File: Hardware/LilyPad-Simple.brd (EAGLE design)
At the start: 50 x 50 mm, 43 parts, among them U1 ATMEGA328P_TQFP, U2 MCP73831, U3 MIC5219 3.3V, Y1 8MHZ

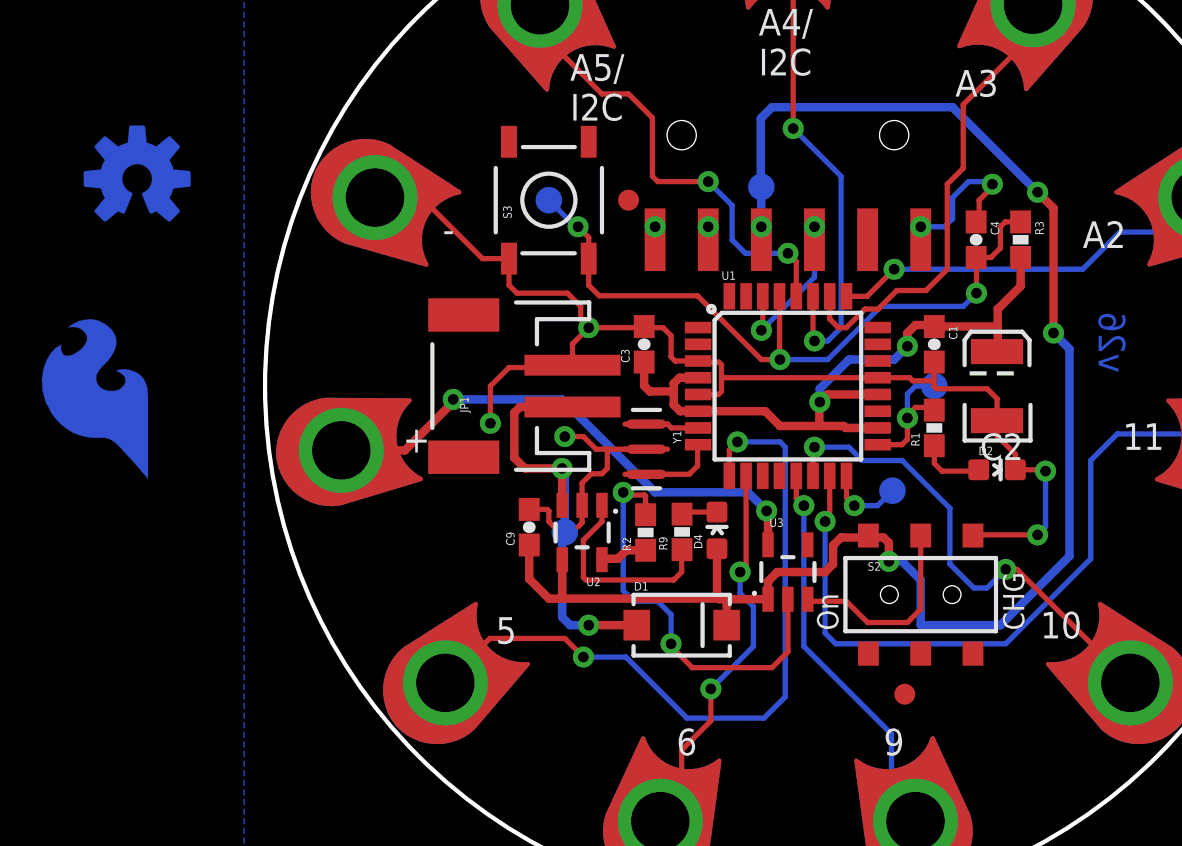
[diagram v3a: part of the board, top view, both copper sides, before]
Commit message: fixed 3.3 routing
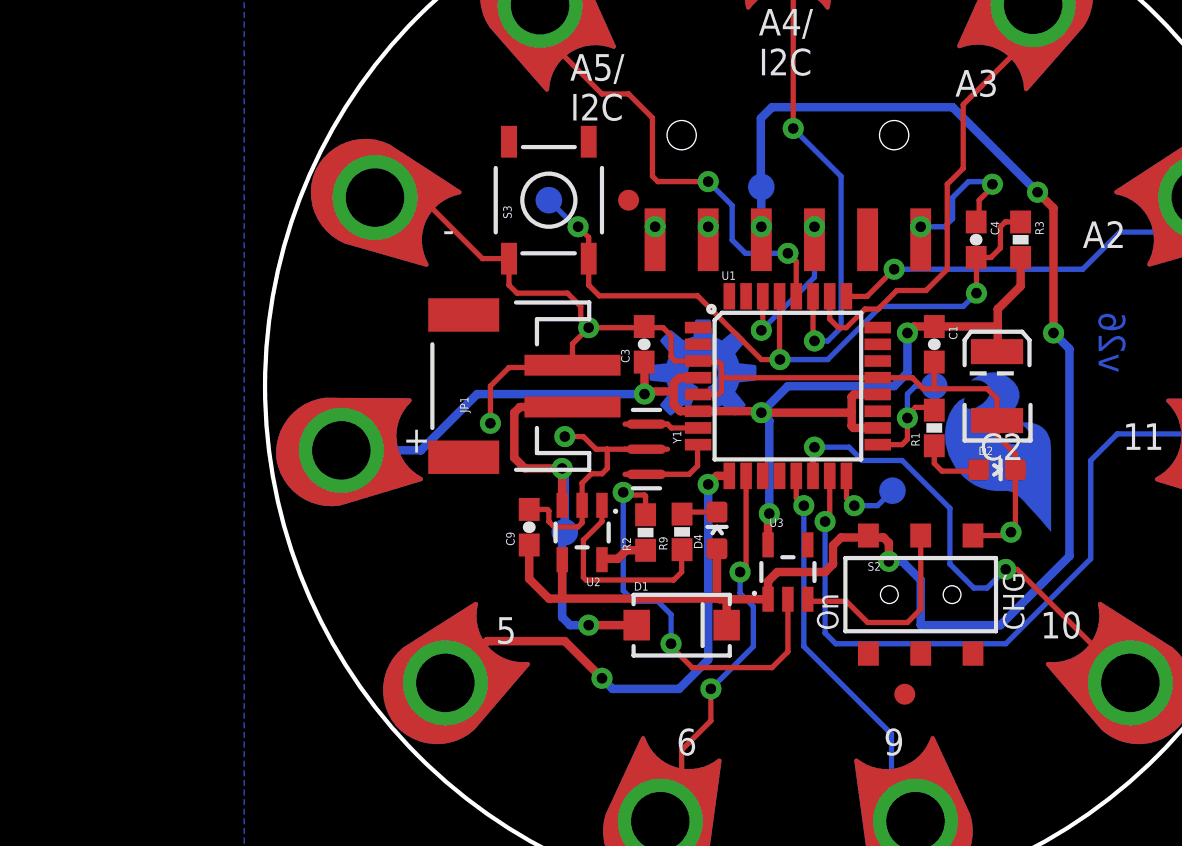
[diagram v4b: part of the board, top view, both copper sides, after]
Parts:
- moved LOGO2 43.3 mm to (13.1, -7.11)
- moved LOGO1 28.6 mm to (-4.06, 0.64)
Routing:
- net D5: track 35.2 -> 24.9 mm
- net GND: track 92.1 -> 90.2 mm, vias 9 -> 8
- net 3.3V: track 60.3 -> 59.1 mm

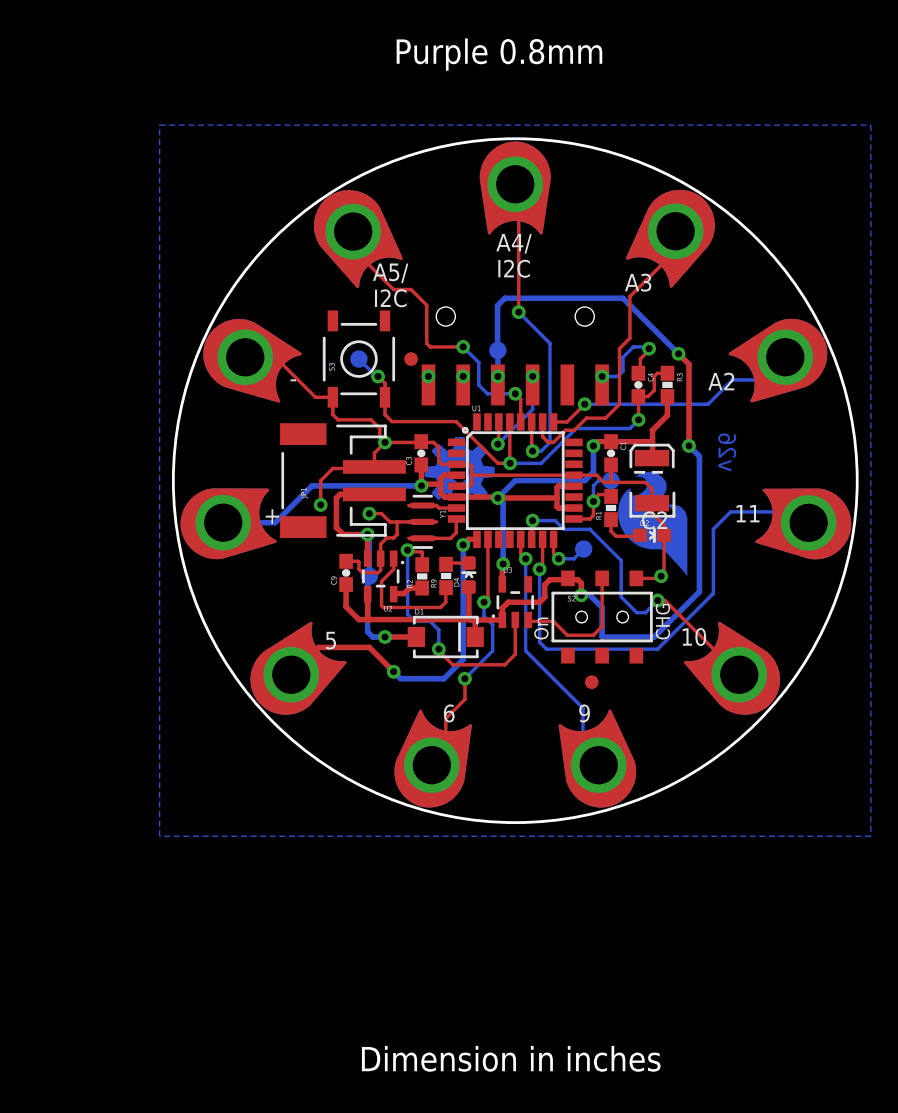
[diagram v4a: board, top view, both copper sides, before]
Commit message: Checklist edits
Silk edited, TX and RX reconnected
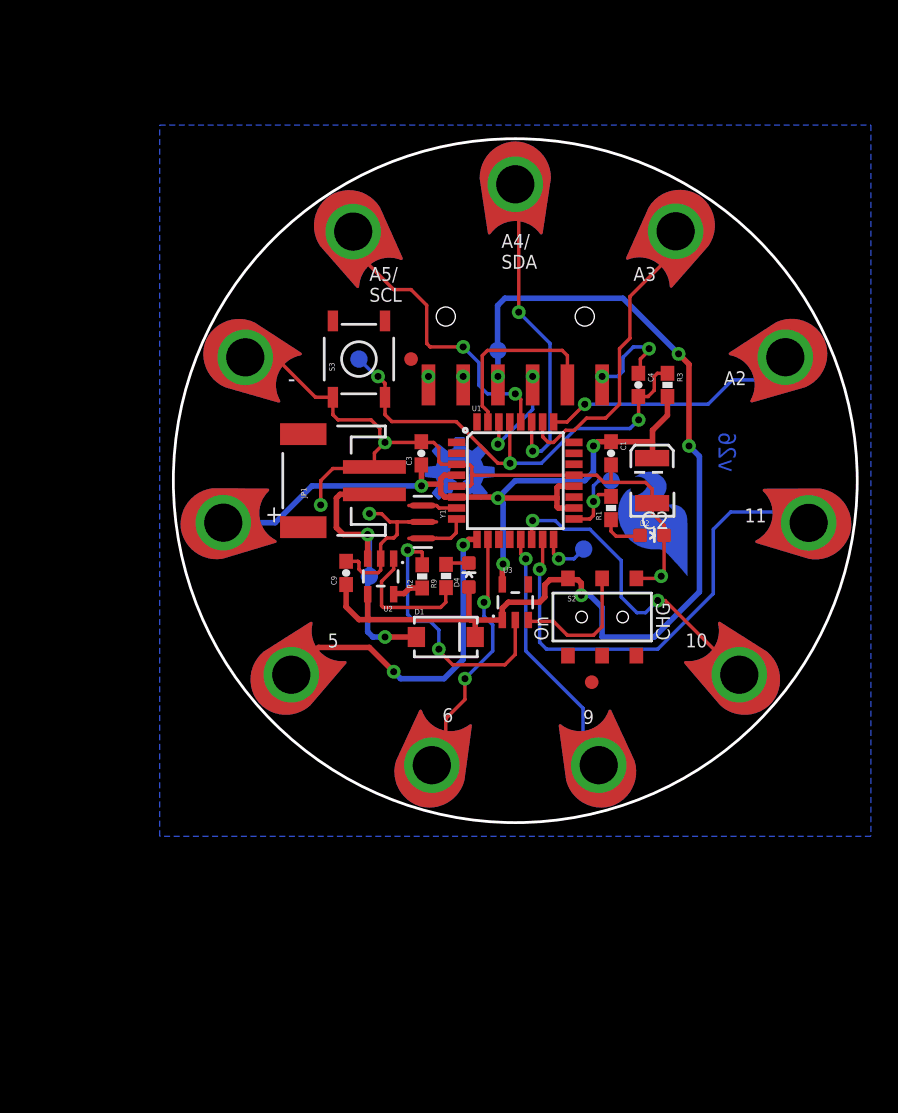
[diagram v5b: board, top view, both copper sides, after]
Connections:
- net DTR: now also JP2.1
- net RXI: now also JP2.3
- net TXO: now also JP2.2
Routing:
- net TXO: track 0.00 -> 13.7 mm
- net RXI: track 7.66 -> 8.28 mm
- net DTR: track 7.17 -> 7.79 mm
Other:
- board text added: "A4/ SDA"
- board text added: "A5/ SCL"
- board text removed: "A4/ I2C"
- board text removed: "A5/ I2C"
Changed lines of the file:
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@@
 <text x="-88.9" y="-3.81" size="1.778" layer="51" font="vector" ratio="15">Dia Campbell</text>
 <text x="14.859" y="0.635" size="1.27" layer="16" font="vector" ratio="15" rot="MR90">v26</text>
-<text x="-18.415" y="-3.175" size="1.27" layer="21" font="vector" ratio="15">+</text>
-<text x="-16.51" y="6.858" size="1.27" layer="21" font="vector" ratio="15">-</text>
-<text x="-10.414" y="12.7" size="1.27" layer="21" font="vector" ratio="15">A5/
-I2C</text>
-<text x="-1.397" y="14.859" size="1.27" layer="21" font="vector" ratio="15">A4/
-I2C</text>
-<text x="8.001" y="13.843" size="1.27" layer="21" font="vector" ratio="15">A3</text>
-<text x="14.097" y="6.604" size="1.27" layer="21" font="vector" ratio="15">A2</text>
-<text x="16.002" y="-3.048" size="1.27" layer="21" font="vector" ratio="15">11</text>
-<text x="12.065" y="-12.065" size="1.27" layer="21" font="vector" ratio="15">10</text>
-<text x="4.572" y="-17.653" size="1.27" layer="21" font="vector" ratio="15">9</text>
-<text x="-5.334" y="-17.653" size="1.27" layer="21" font="vector" ratio="15">6</text>
-<text x="-13.97" y="-12.319" size="1.27" layer="21" font="vector" ratio="15">5</text>
+<text x="-18.288" y="-3.048" size="1.27" layer="21" font="vector" ratio="15">+</text>
+<text x="-16.637" y="6.858" size="1.27" layer="21" font="vector" ratio="15">-</text>
+<text x="-10.668" y="13.081" size="1.016" layer="21" font="vector" ratio="15">A5/
+SCL</text>
+<text x="-1.016" y="15.494" size="1.016" layer="21" font="vector" ratio="15">A4/
+SDA</text>
+<text x="8.636" y="14.605" size="1.016" layer="21" font="vector" ratio="15">A3</text>
+<text x="15.24" y="6.985" size="1.016" layer="21" font="vector" ratio="15">A2</text>
+<text x="16.764" y="-3.048" size="1.016" layer="21" font="vector" ratio="15">11</text>
+<text x="12.446" y="-12.192" size="1.016" layer="21" font="vector" ratio="15">10</text>
+<text x="4.953" y="-17.78" size="1.016" layer="21" font="vector" ratio="15">9</text>
+<text x="-5.334" y="-17.653" size="1.016" layer="21" font="vector" ratio="15">6</text>
+<text x="-13.716" y="-12.192" size="1.016" layer="21" font="vector" ratio="15">5</text>
 <text x="2.413" y="-11.684" size="1.016" layer="21" font="vector" ratio="15" rot="R90">On</text>
 <text x="10.287" y="-8.89" size="1.016" layer="21" font="vector" ratio="15" rot="R270">CHG</text>
 <dimension x1="25" y1="0" x2="-25" y2="0" x3="0" y3="-38.1" textsize="1.778" textratio="15" layer="47" dtype="diameter" unit="inch"/>
-<text x="-11.43" y="-43.18" size="1.778" layer="20" font="vector" ratio="15">Dimension in inches</text>
-<text x="-8.89" y="30.48" size="1.778" layer="20" font="vector" ratio="15">Purple 0.8mm</text>
+<text x="-11.43" y="-43.18" size="1.778" layer="47" font="vector" ratio="15">Dimension in inches</text>
+<text x="-8.89" y="30.48" size="1.778" layer="51" font="vector" ratio="15">Purple 0.8mm</text>
 </plain>
 <attributes>
@@
 <wire x1="-1.2" y1="4.2926" x2="-1.2" y2="2.737" width="0.254" layer="1"/>
 <wire x1="-1.2" y1="2.737" x2="-1.27" y2="2.667" width="0.254" layer="1"/>
+<contactref element="JP2" pad="3"/>
+<wire x1="1.27" y1="7.62" x2="1.27" y2="7" width="0.254" layer="1"/>
 </signal>
 <signal name="TXO">
 <contactref element="U1" pad="31"/>
+<contactref element="JP2" pad="2"/>
+<wire x1="-2" y1="4.2926" x2="-2" y2="5.048" width="0.254" layer="1"/>
+<wire x1="-2" y1="5.048" x2="-2.413" y2="5.461" width="0.254" layer="1"/>
+<wire x1="-2.413" y1="5.461" x2="-2.413" y2="9.144" width="0.254" layer="1"/>
+<wire x1="-2.413" y1="9.144" x2="-2.032" y2="9.525" width="0.254" layer="1"/>
+<wire x1="-2.032" y1="9.525" x2="3.429" y2="9.525" width="0.254" layer="1"/>
+<wire x1="3.429" y1="9.525" x2="3.81" y2="9.144" width="0.254" layer="1"/>
+<wire x1="3.81" y1="9.144" x2="3.81" y2="7" width="0.254" layer="1"/>
 </signal>
 <signal name="D5">
@@
 <wire x1="9.144" y1="8.89" x2="9.144" y2="7.994" width="0.254" layer="1"/>
 <wire x1="9.144" y1="7.994" x2="9" y2="7.85" width="0.254" layer="1"/>
+<contactref element="JP2" pad="1"/>
+<wire x1="6.35" y1="7.62" x2="6.35" y2="7" width="0.254" layer="1"/>
 </signal>
 <signal name="D6">
